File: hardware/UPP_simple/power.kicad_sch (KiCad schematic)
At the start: 14 parts, among them J37 Conn_01x02, U10 MCP1700x-330xxMB, U6 LM2596S-5, U7 LM2596S-12

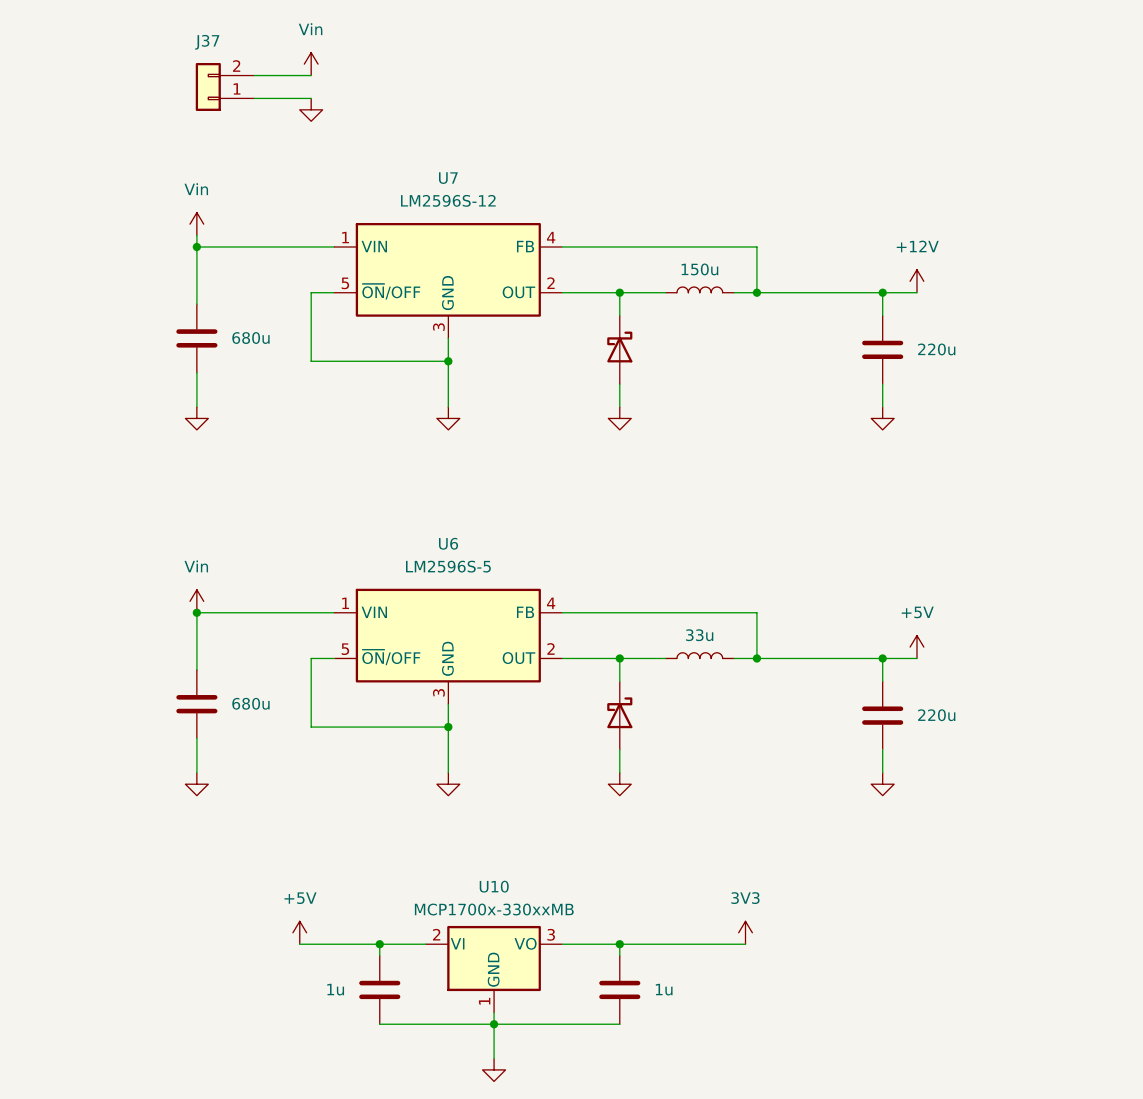
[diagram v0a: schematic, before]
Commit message: Solved ERC errors and cleaned up schematic
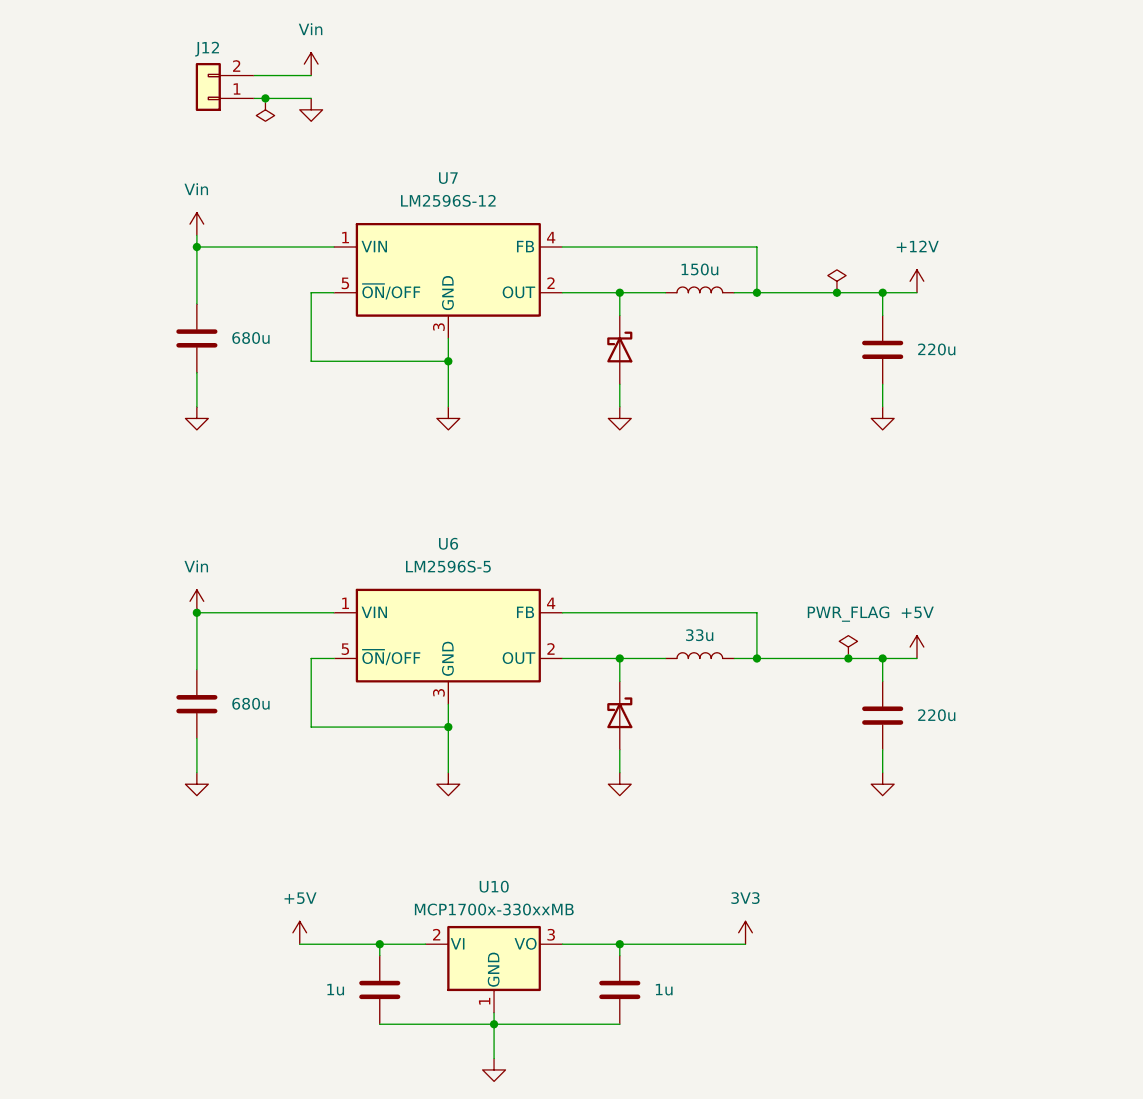
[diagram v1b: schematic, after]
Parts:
- removed J37: Conn_01x02, symbol Connector_Generic:Conn_01x02
- added J12: Conn_01x02, symbol Connector_Generic:Conn_01x02
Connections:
- net GND: now also J12.1 (Pin_1)
- net Vin: now also J12.2 (Pin_2)

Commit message: Add files via upload
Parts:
- removed C3, C6: 220u, Capacitor_SMD:C_0603_1608Metric_Pad1.08x0.95mm_HandSolder, symbol Device:C
- removed C4, C5: 680u, symbol Device:C
- removed D13, D14: D_Schottky, symbol Device:D_Schottky
- removed L1: 33u, symbol Device:L
- removed L2: 150u, symbol Device:L
- removed U6: LM2596S-5, Package_TO_SOT_SMD:TO-263-5_TabPin3, symbol Regulator_Switching:LM2596S-5
- removed U7: LM2596S-12, Package_TO_SOT_SMD:TO-263-5_TabPin3, symbol Regulator_Switching:LM2596S-12
- added C1: 1u, Capacitor_SMD:C_0805_2012Metric, symbol Device:C
- added C2, C4, C5: 1u, Capacitor_SMD:C_0805_2012Metric, symbol PUTM_EV_IMD_SAFETY_2021-rescue:C-Device
- added C3: 100n, Capacitor_SMD:C_0603_1608Metric, symbol Device:C_Small
- added C6: 100n, Capacitor_SMD:C_0603_1608Metric, symbol PUTM_EV_IMD_SAFETY_2021-rescue:C-Device
- added D15: LBD52A24L01, Diode_SMD:D_SOD-523, symbol Diode:1N630xCA
- added F1: 500mA, Diode_SMD:D_1812_4532Metric_Pad1.30x3.40mm_HandSolder, symbol Device:Fuse
- added U5: MC78M12CDTG, Package_TO_SOT_SMD:TO-252-3_TabPin2, symbol PUTM_EV_IMD_SAFETY_2021-rescue:MC78M05_TO252-Regulator_Linear
- added U8: LM1117IMP-5.0, Package_TO_SOT_SMD:SOT-223-3_TabPin2, symbol PUTM_EV_IMD_SAFETY_2021-rescue:LM1117-5.0-Regulator_Linear
- renumbered C8 to C7, C7 to C8
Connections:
- net +12V: now also C2.1, C3.1, C4.1, U5.3 (VO), U8.3 (VI)
- net +5V: now also C5.1, C6.1, U8.2 (VO)
- net GND: now also C1.2, C2.2, C3.2, C4.2, C5.2, C6.2, D15.2 (A2), U5.2 (GND), U8.1 (GND)
- net Vin: no longer names the net of J12.2 (Pin_2)
- net Vin: now also F1.1
- new net: C1.1, D15.1 (A1), F1.2, U5.1 (VI)
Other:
- moved on the sheet: J12, U10
